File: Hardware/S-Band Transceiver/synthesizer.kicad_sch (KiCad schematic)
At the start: 55 parts, among them J1 SMA, J2 SMA, U1 ADF4351, X1 XO32

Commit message: Starting to route board
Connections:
- net LO+: now also L6.2; no longer L5.2
- net LO-: now also L5.2; no longer L6.2
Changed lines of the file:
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@@
 	(global_label "LO-"
 		(shape input)
+		(at 248.92 63.5 0)
+		(fields_autoplaced yes)
+		(effects
+			(font
+				(size 1.27 1.27)
+			)
+			(justify left)
+		)
+		(property "Intersheetrefs" "${INTERSHEET_REFS}"
+			(at 255.8362 63.5 0)
+			(effects
+				(font
+					(size 1.27 1.27)
+				)
+				(justify left)
+				(hide yes)
+			)
+		)
+	)
+	(global_label "REF_IN"
+		(shape input)
+		(at 114.3 104.14 180)
+		(fields_autoplaced yes)
+		(effects
+			(font
+				(size 1.27 1.27)
+			)
+			(justify right)
+		)
+		(property "Intersheetrefs" "${INTERSHEET_REFS}"
+			(at 104.9043 104.14 0)
+			(effects
+				(font
+					(size 1.27 1.27)
+				)
+				(justify right)
+				(hide yes)
+			)
+		)
+	)
+	(global_label "LD"
+		(shape input)
+		(at 179.07 63.5 90)
+		(fields_autoplaced yes)
+		(effects
+			(font
+				(size 1.27 1.27)
+			)
+			(justify left)
+		)
+		(property "Intersheetrefs" "${INTERSHEET_REFS}"
+			(at 179.07 58.2167 90)
+			(effects
+				(font
+					(size 1.27 1.27)
+				)
+				(justify left)
+				(hide yes)
+			)
+		)
+	)
+	(global_label "SYNTH_EN"
+		(shape input)
+		(at 104.14 96.52 180)
+		(fields_autoplaced yes)
+		(effects
+			(font
+				(size 1.27 1.27)
+			)
+			(justify right)
+		)
+		(property "Intersheetrefs" "${INTERSHEET_REFS}"
+			(at 91.781 96.52 0)
+			(effects
+				(font
+					(size 1.27 1.27)
+				)
+				(justify right)
+				(hide yes)
+			)
+		)
+	)
+	(global_label "REF_IN"
+		(shape input)
+		(at 63.5 40.64 0)
+		(fields_autoplaced yes)
+		(effects
+			(font
+				(size 1.27 1.27)
+			)
+			(justify left)
+		)
+		(property "Intersheetrefs" "${INTERSHEET_REFS}"
+			(at 72.8957 40.64 0)
+			(effects
+				(font
+					(size 1.27 1.27)
+				)
+				(justify left)
+				(hide yes)
+			)
+		)
+	)
+	(global_label "MUXOUT"
+		(shape input)
+		(at 172.72 86.36 0)
+		(fields_autoplaced yes)
+		(effects
+			(font
+				(size 1.27 1.27)
+			)
+			(justify left)
+		)
+		(property "Intersheetrefs" "${INTERSHEET_REFS}"
+			(at 183.3252 86.36 0)
+			(effects
+				(font
+					(size 1.27 1.27)
+				)
+				(justify left)
+				(hide yes)
+			)
+		)
+	)
+	(global_label "MOSI"
+		(shape input)
+		(at 118.11 83.82 90)
+		(fields_autoplaced yes)
+		(effects
+			(font
+				(size 1.27 1.27)
+			)
+			(justify left)
+		)
+		(property "Intersheetrefs" "${INTERSHEET_REFS}"
+			(at 118.11 76.2386 90)
+			(effects
+				(font
+					(size 1.27 1.27)
+				)
+				(justify left)
+				(hide yes)
+			)
+		)
+	)
+	(global_label "SYNTH_TX"
+		(shape input)
+		(at 250.19 130.81 0)
+		(fields_autoplaced yes)
+		(effects
+			(font
+				(size 1.27 1.27)
+			)
+			(justify left)
+		)
+		(property "Intersheetrefs" "${INTERSHEET_REFS}"
+			(at 262.2466 130.81 0)
+			(effects
+				(font
+					(size 1.27 1.27)
+				)
+				(justify left)
+				(hide yes)
+			)
+		)
+	)
+	(global_label "EXT_REF"
+		(shape input)
+		(at 60.96 50.8 270)
+		(fields_autoplaced yes)
+		(effects
+			(font
+				(size 1.27 1.27)
+			)
+			(justify right)
+		)
+		(property "Intersheetrefs" "${INTERSHEET_REFS}"
+			(at 60.96 61.5865 90)
+			(effects
+				(font
+					(size 1.27 1.27)
+				)
+				(justify right)
+				(hide yes)
+			)
+		)
+	)
+	(global_label "LO+"
+		(shape input)
 		(at 248.92 81.28 0)
 		(fields_autoplaced yes)
@@
 			(effects
 				(font
-					(size 1.27 1.27)
-				)
-				(justify left)
-				(hide yes)
-			)
-		)
-	)
-	(global_label "REF_IN"
-		(shape input)
-		(at 114.3 104.14 180)
-		(fields_autoplaced yes)
-		(effects
-			(font
-				(size 1.27 1.27)
-			)
-			(justify right)
-		)
-		(property "Intersheetrefs" "${INTERSHEET_REFS}"
-			(at 104.9043 104.14 0)
-			(effects
-				(font
-					(size 1.27 1.27)
-				)
-				(justify right)
-				(hide yes)
-			)
-		)
-	)
-	(global_label "LD"
-		(shape input)
-		(at 179.07 63.5 90)
-		(fields_autoplaced yes)
-		(effects
-			(font
-				(size 1.27 1.27)
-			)
-			(justify left)
-		)
-		(property "Intersheetrefs" "${INTERSHEET_REFS}"
-			(at 179.07 58.2167 90)
-			(effects
-				(font
-					(size 1.27 1.27)
-				)
-				(justify left)
-				(hide yes)
-			)
-		)
-	)
-	(global_label "SYNTH_EN"
-		(shape input)
-		(at 104.14 96.52 180)
-		(fields_autoplaced yes)
-		(effects
-			(font
-				(size 1.27 1.27)
-			)
-			(justify right)
-		)
-		(property "Intersheetrefs" "${INTERSHEET_REFS}"
-			(at 91.781 96.52 0)
-			(effects
-				(font
-					(size 1.27 1.27)
-				)
-				(justify right)
-				(hide yes)
-			)
-		)
-	)
-	(global_label "REF_IN"
-		(shape input)
-		(at 63.5 40.64 0)
-		(fields_autoplaced yes)
-		(effects
-			(font
-				(size 1.27 1.27)
-			)
-			(justify left)
-		)
-		(property "Intersheetrefs" "${INTERSHEET_REFS}"
-			(at 72.8957 40.64 0)
-			(effects
-				(font
-					(size 1.27 1.27)
-				)
-				(justify left)
-				(hide yes)
-			)
-		)
-	)
-	(global_label "MUXOUT"
-		(shape input)
-		(at 172.72 86.36 0)
-		(fields_autoplaced yes)
-		(effects
-			(font
-				(size 1.27 1.27)
-			)
-			(justify left)
-		)
-		(property "Intersheetrefs" "${INTERSHEET_REFS}"
-			(at 183.3252 86.36 0)
-			(effects
-				(font
-					(size 1.27 1.27)
-				)
-				(justify left)
-				(hide yes)
-			)
-		)
-	)
-	(global_label "MOSI"
-		(shape input)
-		(at 118.11 83.82 90)
-		(fields_autoplaced yes)
-		(effects
-			(font
-				(size 1.27 1.27)
-			)
-			(justify left)
-		)
-		(property "Intersheetrefs" "${INTERSHEET_REFS}"
-			(at 118.11 76.2386 90)
-			(effects
-				(font
-					(size 1.27 1.27)
-				)
-				(justify left)
-				(hide yes)
-			)
-		)
-	)
-	(global_label "SYNTH_TX"
-		(shape input)
-		(at 250.19 130.81 0)
-		(fields_autoplaced yes)
-		(effects
-			(font
-				(size 1.27 1.27)
-			)
-			(justify left)
-		)
-		(property "Intersheetrefs" "${INTERSHEET_REFS}"
-			(at 262.2466 130.81 0)
-			(effects
-				(font
-					(size 1.27 1.27)
-				)
-				(justify left)
-				(hide yes)
-			)
-		)
-	)
-	(global_label "EXT_REF"
-		(shape input)
-		(at 60.96 50.8 270)
-		(fields_autoplaced yes)
-		(effects
-			(font
-				(size 1.27 1.27)
-			)
-			(justify right)
-		)
-		(property "Intersheetrefs" "${INTERSHEET_REFS}"
-			(at 60.96 61.5865 90)
-			(effects
-				(font
-					(size 1.27 1.27)
-				)
-				(justify right)
-				(hide yes)
-			)
-		)
-	)
-	(global_label "LO+"
-		(shape input)
-		(at 248.92 63.5 0)
-		(fields_autoplaced yes)
-		(effects
-			(font
-				(size 1.27 1.27)
-			)
-			(justify left)
-		)
-		(property "Intersheetrefs" "${INTERSHEET_REFS}"
-			(at 255.8362 63.5 0)
-			(effects
-				(font

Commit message: Updating routing
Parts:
- added R66: 10k, Resistor_SMD:R_0603_1608Metric, symbol Device:R_Small_US
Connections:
- net +3.3VA: now also R66.1
- net PDB_RF: no longer names the net of U1.26 (PDB_RF)
- net PDB_RF: now also R66.2
- net SYNTH_EN: no longer names the net of R3.1, U1.4 (CE)
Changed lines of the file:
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@@
 	)
 	(junction
-		(at 106.68 96.52)
-		(diameter 0)
-		(color 0 0 0 0)
-	)
-	(junction
 		(at 147.32 54.61)
 		(diameter 0)
@@
 	)
 	(junction
+		(at 106.68 86.36)
+		(diameter 0)
+		(color 0 0 0 0)
+	)
+	(junction
 		(at 180.34 116.84)
 		(diameter 0)
@@
 	(wire
 		(pts
+			(xy 106.68 85.09) (xy 106.68 86.36)
+		)
+		(stroke
+			(width 0)
+			(type default)
+		)
+	)
+	(wire
+		(pts
 			(xy 143.51 132.08) (xy 144.78 132.08)
 		)
@@
 	(wire
 		(pts
+			(xy 102.87 86.36) (xy 106.68 86.36)
+		)
+		(stroke
+			(width 0)
+			(type default)
+		)
+	)
+	(wire
+		(pts
 			(xy 147.32 129.54) (xy 147.32 132.08)
 		)
@@
 	(wire
 		(pts
+			(xy 102.87 99.06) (xy 124.46 99.06)
+		)
+		(stroke
+			(width 0)
+			(type default)
+		)
+	)
+	(wire
+		(pts
 			(xy 149.86 132.08) (xy 152.4 132.08)
 		)
@@
 	(wire
 		(pts
-			(xy 121.92 99.06) (xy 124.46 99.06)
-		)
-		(stroke
-			(width 0)
-			(type default)
-		)
-	)
-	(wire
-		(pts
 			(xy 215.9 68.58) (xy 219.71 68.58)
 		)
@@
 	(wire
 		(pts
-			(xy 134.62 62.23) (xy 134.62 64.77)
+			(xy 102.87 86.36) (xy 102.87 88.9)
 		)
 		(stroke
@@
 	(wire
 		(pts
-			(xy 104.14 96.52) (xy 106.68 96.52)
+			(xy 134.62 62.23) (xy 134.62 64.77)
 		)
 		(stroke
@@
 	(wire
 		(pts
+			(xy 102.87 93.98) (xy 102.87 99.06)
+		)
+		(stroke
+			(width 0)
+			(type default)
+		)
+	)
+	(wire
+		(pts
 			(xy 219.71 72.39) (xy 215.9 72.39)
 		)
@@
 		)
 	)
-	(global_label "PDB_RF"
-		(shape input)
-		(at 121.92 99.06 180)
-		(fields_autoplaced yes)
-		(effects
-			(font
-				(size 1.27 1.27)
-			)
-			(justify right)
-		)
-		(property "Intersheetrefs" "${INTERSHEET_REFS}"
-			(at 111.7986 99.06 0)
-			(effects
-				(font
-					(size 1.27 1.27)
-				)
-				(justify right)
-				(hide yes)
-			)
-		)
-	)
 	(global_label "~{SYNTH_CS}"
 		(shape input)
@@
 		)
 	)
-	(global_label "SYNTH_EN"
-		(shape input)
-		(at 104.14 96.52 180)
-		(fields_autoplaced yes)
-		(effects
-			(font
-				(size 1.27 1.27)
-			)
-			(justify right)
-		)
-		(property "Intersheetrefs" "${INTERSHEET_REFS}"
-			(at 91.781 96.52 0)
-			(effects
-				(font
-					(size 1.27 1.27)
-				)
-				(justify right)
-				(hide yes)
-			)
-		)
-	)
 	(global_label "REF_IN"
 		(shape input)
@@
 	)
 	(symbol
+		(lib_id "Device:R_Small_US")
+		(at 102.87 91.44 0)
+		(unit 1)
+		(exclude_from_sim no)
+		(in_bom yes)
+		(on_board yes)
+		(dnp no)
+		(property "Reference" "R66"
+			(at 99.822 90.17 0)
+			(effects
+				(font
+					(size 1.27 1.27)
+				)
+			)
+		)
+		(property "Value" "10k"
+			(at 100.076 92.456 0)
+			(effects
+				(font
+					(size 1.27 1.27)
+				)
+			)
+		)
+		(property "Footprint" "Resistor_SMD:R_0603_1608Metric"
+			(at 102.87 91.44 0)
+			(effects
+				(font
+					(size 1.27 1.27)
+				)
+				(hide yes)
+			)
+		)
+		(property "Datasheet" "~"
+			(at 102.87 91.44 0)
+			(effects
+				(font
+					(size 1.27 1.27)
+				)
+				(hide yes)
+			)
+		)
+		(property "Description" "Resistor, small US symbol"
+			(at 102.87 91.44 0)
+			(effects
+				(font
+					(size 1.27 1.27)
+				)
+				(hide yes)
+			)
+		)
+		(pin "2"
+		)
+		(pin "1"
+		)
+		(instances
+			(project "S-Band Transceiver"
+				(path "/811f57cf-e3df-4fba-aff9-353adc85299e/1f8ad4e6-608c-455a-8c5c-ffe69657f316"
+					(reference "R66")
+					(unit 1)
+				)
+			)
+		)
+	)
+	(symbol
 		(lib_id "Device:C_Small")
 		(at 190.5 121.92 180)
@@
 	(symbol
 		(lib_id "power:+3.3VA")
-		(at 106.68 86.36 0)
+		(at 106.68 85.09 0)
 		(unit 1)
 		(exclude_from_sim no)
@@
 		(dnp no)
 		(property "Reference" "#PWR07"
-			(at 106.68 90.17 0)
+			(at 106.68 88.9 0)
 			(effects
 				(font
@@
 		)
 		(property "Value" "+3.3VA"
-			(at 106.68 82.042 0)
+			(at 106.68 80.772 0)
 			(effects
 				(font
@@
 		)
 		(property "Footprint" ""
-			(at 106.68 86.36 0)
+			(at 106.68 85.09 0)
 			(effects
 				(font
@@
 		)
 		(property "Datasheet" ""
-			(at 106.68 86.36 0)
+			(at 106.68 85.09 0)
 			(effects
 				(font
@@
 		)
 		(property "Description" "Power symbol creates a global label with name \"+3.3VA\""
-			(at 106.68 86.36 0)
+			(at 106.68 85.09 0)
 			(effects
 				(font

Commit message: Updates to schematic
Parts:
- J1, J2: value SMA -> SMA-J-P-H-ST-EM1; Digikey (none) -> SAM8857-ND
- U1: Digikey (none) -> 505-ADF4351BCPZ-RL7CT-ND
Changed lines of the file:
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@@
 			)
 		)
-		(property "Value" "SMA"
+		(property "Value" "SMA-J-P-H-ST-EM1"
 			(at 259.08 114.5931 0)
 			(effects
@@
 			)
 		)
-		(property "Datasheet" " ~"
+		(property "Datasheet" "https://mm.digikey.com/Volume0/opasdata/d220001/medias/docus/6129/sma-j-p-x-st-em1-mkt.pdf"
 			(at 255.27 113.03 0)
 			(effects
@@
 			)
 		)
+		(property "Digikey" "SAM8857-ND"
+			(at 255.27 113.03 0)
+			(effects
+				(font
+					(size 1.27 1.27)
+				)
+				(hide yes)
+			)
+		)
 		(pin "1"
 		)
@@
 			)
 		)
+		(property "Digikey" "505-ADF4351BCPZ-RL7CT-ND"
+			(at 144.78 101.6 0)
+			(effects
+				(font
+					(size 1.27 1.27)
+				)
+				(hide yes)
+			)
+		)
 		(pin "11"
 		)
@@
 			)
 		)
-		(property "Value" "SMA"
+		(property "Value" "SMA-J-P-H-ST-EM1"
 			(at 73.66 51.0931 0)
 			(effects
@@
 			)
 		)
-		(property "Datasheet" " ~"
+		(property "Datasheet" "https://mm.digikey.com/Volume0/opasdata/d220001/medias/docus/6129/sma-j-p-x-st-em1-mkt.pdf"
 			(at 69.85 49.53 0)
 			(effects
@@
 			(at 69.85 49.53 0)
 			(effects
+				(font
+					(size 1.27 1.27)
+				)
+				(hide yes)
+			)
+		)
+		(property "Digikey" "SAM8857-ND"
+			(at 69.85 49.53 0)
+			(effects

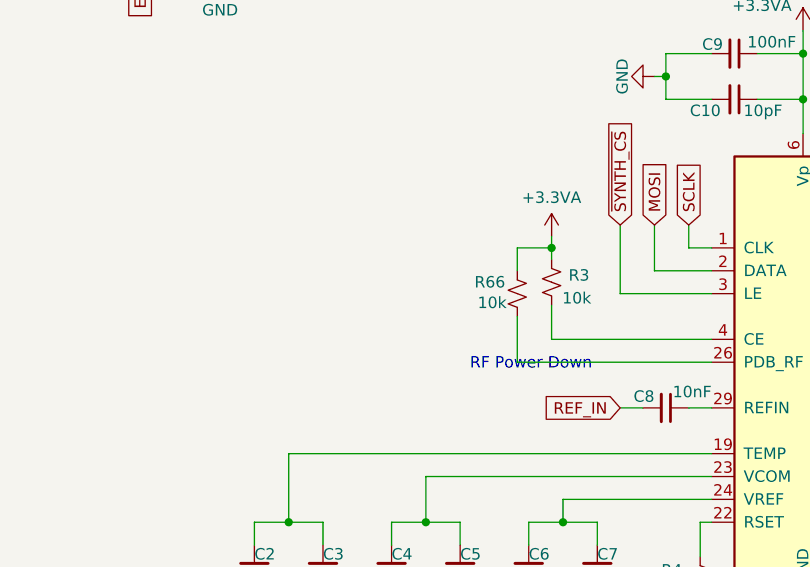
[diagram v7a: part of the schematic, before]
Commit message: Updating notes in schematic
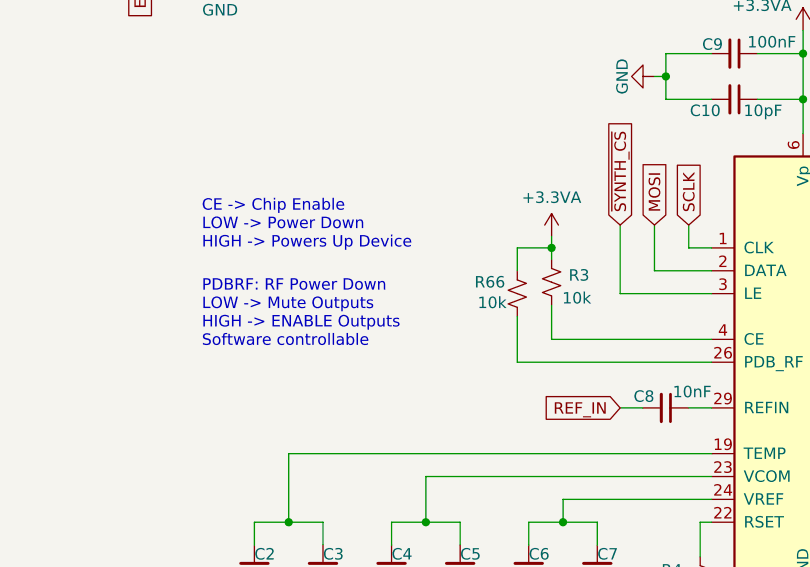
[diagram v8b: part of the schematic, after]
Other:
- note added: "CE -> Chip Enable LOW -> Power Down HIGH -> Powers Up Device"
- note added: "PDBRF: RF Power Down LOW -> Mute Outputs HIGH -> ENABLE Outputs Software controllable"
- note removed: "RF Power Down"
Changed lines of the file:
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@@
 		)
 	)
-	(text "RF Power Down"
+	(text "PDBRF: RF Power Down\nLOW -> Mute Outputs\nHIGH -> ENABLE Outputs\nSoftware controllable"
 		(exclude_from_sim no)
-		(at 104.394 99.314 0)
+		(at 67.818 93.726 0)
 		(effects
 			(font
 				(size 1.27 1.27)
 			)
+			(justify left)
 		)
 	)
+	(text "CE -> Chip Enable\nLOW -> Power Down\nHIGH -> Powers Up Device"
+		(exclude_from_sim no)
+		(at 67.818 83.82 0)
+		(effects
+			(font
+				(size 1.27 1.27)
+			)
+			(justify left)
+		)
+	)
